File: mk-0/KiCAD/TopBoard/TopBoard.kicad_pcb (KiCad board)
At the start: 2 copper layers, 88 x 88 mm, 177 parts, among them J1 Conn_01x04, J2 Conn_01x04, J3 USB_C_Receptacle_USB2.0_16P, J4 Conn_01x15, J5 Raspberry_Pi_2_3, Q1 AO3400A, SW1 SW_Push, SW2 SW_Push, SW3 SW_Push, SW4 SW_Push, U1 SN74LVC1G126DBV, U10 SRV05-4, U11 AMS1117-1.2, U2 74LVC1G17, U3 SN74LVC2G74, U4 74AHCT1G125, U5 W25Q16JVSS, U6 CAT24C256, U7 SN74LVC1G126DBV, U8 ZL38063, U9 AMS1117-3.3, Y1 12MHz

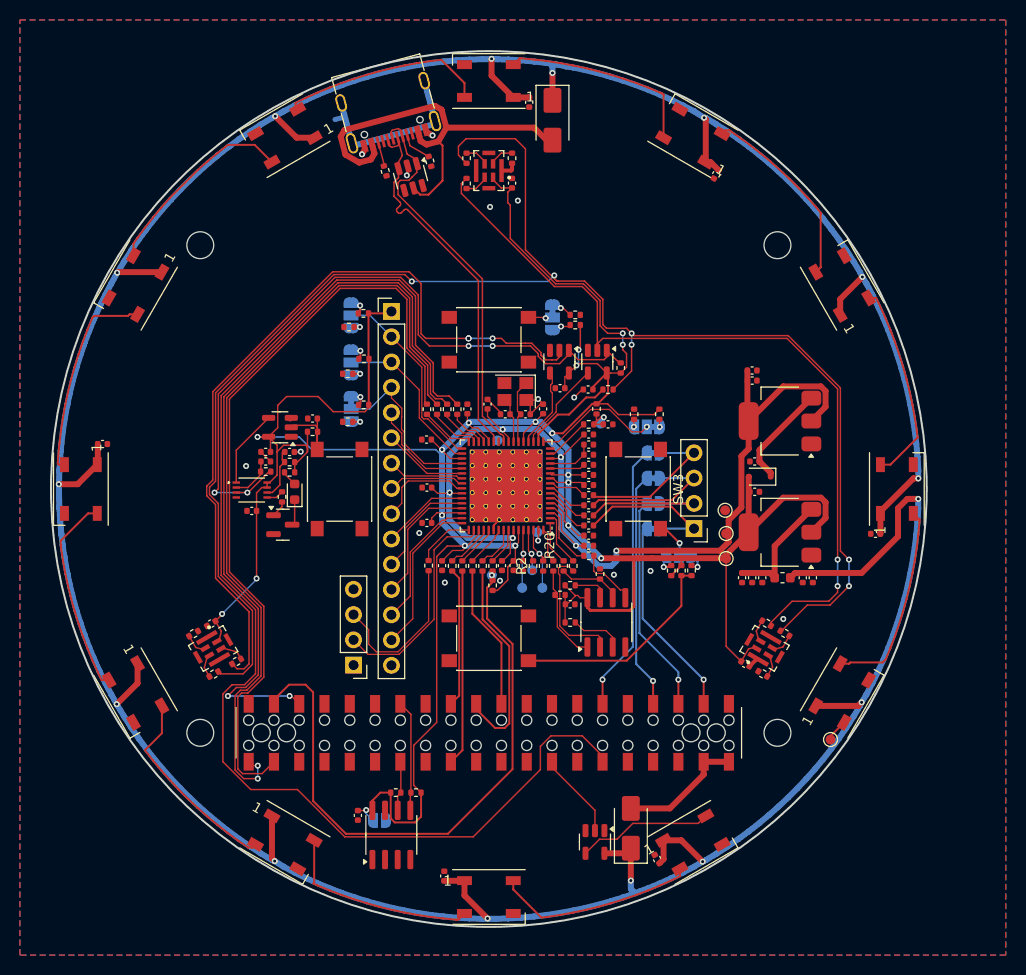
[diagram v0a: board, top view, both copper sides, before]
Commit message: Full routed and DRC completed
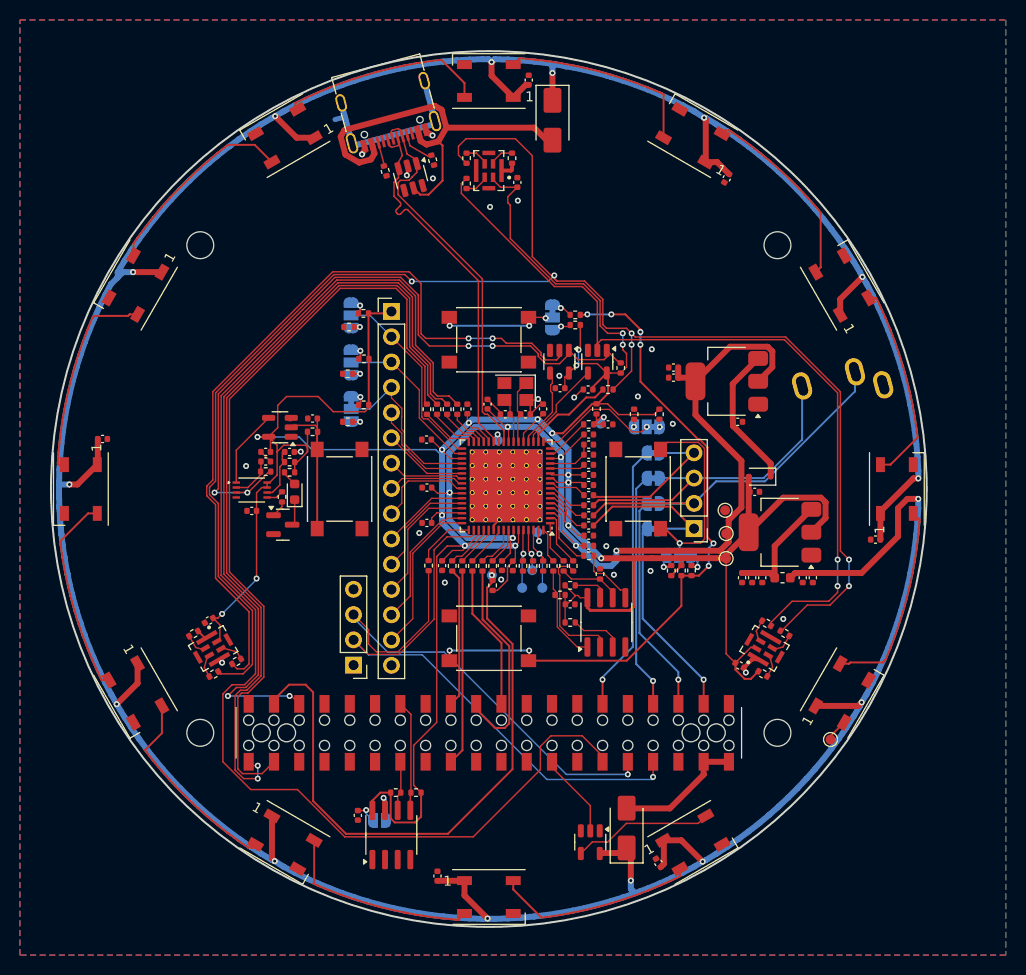
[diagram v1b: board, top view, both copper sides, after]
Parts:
- added J6: AudioJack3, Connector_Audio:Jack_3.5mm_CUI_SJ1-3533NG_Horizontal, B.Cu at (124.8, 59.5)
- moved C47 8.02 mm to (103.8, 57.8), turned to 180 degrees
- moved C49 7.94 mm to (103.8, 58.8), turned to 180 degrees
- moved U11 6.67 mm to (109.1, 59.2)
- moved C45 4.34 mm to (110.2, 63.2), turned to 0 degrees
- moved C28 2.24 mm to (89.2, 28.9), turned to 90 degrees
- moved C22 1.13 mm to (109.1, 38.8)
- moved C39 0.69 mm to (80.1, 108.9)
- moved C41 0.61 mm to (110.4, 87.7)
- moved C38 0.58 mm to (124.1, 75.1)
- moved C40 0.54 mm to (88.1, 39.2)
- moved C32 0.51 mm to (46.4, 65.0)
- moved U4 0.47 mm to (95.4, 105.5)
- moved D16 0.43 mm to (99.1, 104.1)
- moved C37 0.40 mm to (102.3, 107.6)
- moved C42 0.38 mm to (57.1, 83.2)
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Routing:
- net BTN3: track 21.7 -> 67.7 mm, vias 0 -> 8
- net ZL38063_UART_RX: track 22.2 -> 59.9 mm, vias 0 -> 1
- net ZL38063_UART_TX: track 16.3 -> 51.6 mm, vias 0 -> 1
- net ZL38063_DAC1_P: track 14.0 -> 36.8 mm
- net ZL38063_DAC2_P: track 14.7 -> 32.5 mm
- net Net-(JP11-C): track 2.86 -> 19.6 mm
- net Net-(JP10-C): track 1.76 -> 11.3 mm, vias 1 -> 3
- net Net-(C2-Pad1): track 7.19 -> 15.1 mm
- net +3V3: track 331.5 -> 336.9 mm
- net Net-(D15-K): track 10.5 -> 14.5 mm
- net +5V: track 366.7 -> 370.6 mm
- net Net-(JP1-A): track 0.00 -> 3.47 mm, vias 0 -> 1
- net +1V2: track 106.9 -> 110.1 mm
- net GND: track 15.4 -> 18.4 mm, vias 15 -> 23
- net Net-(U8-RTN): track 0.00 -> 1.35 mm, vias 0 -> 1
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
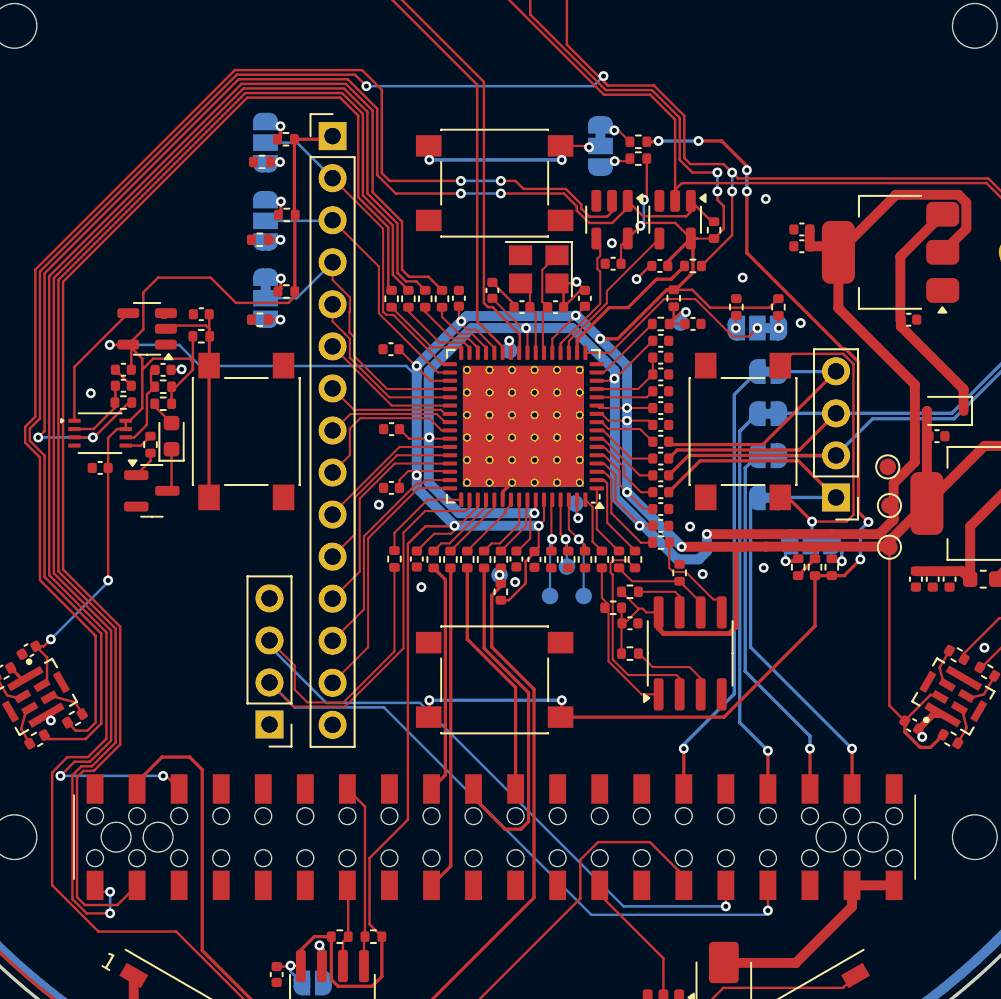
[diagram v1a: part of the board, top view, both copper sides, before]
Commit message: Added 3.5mm Jack to top board
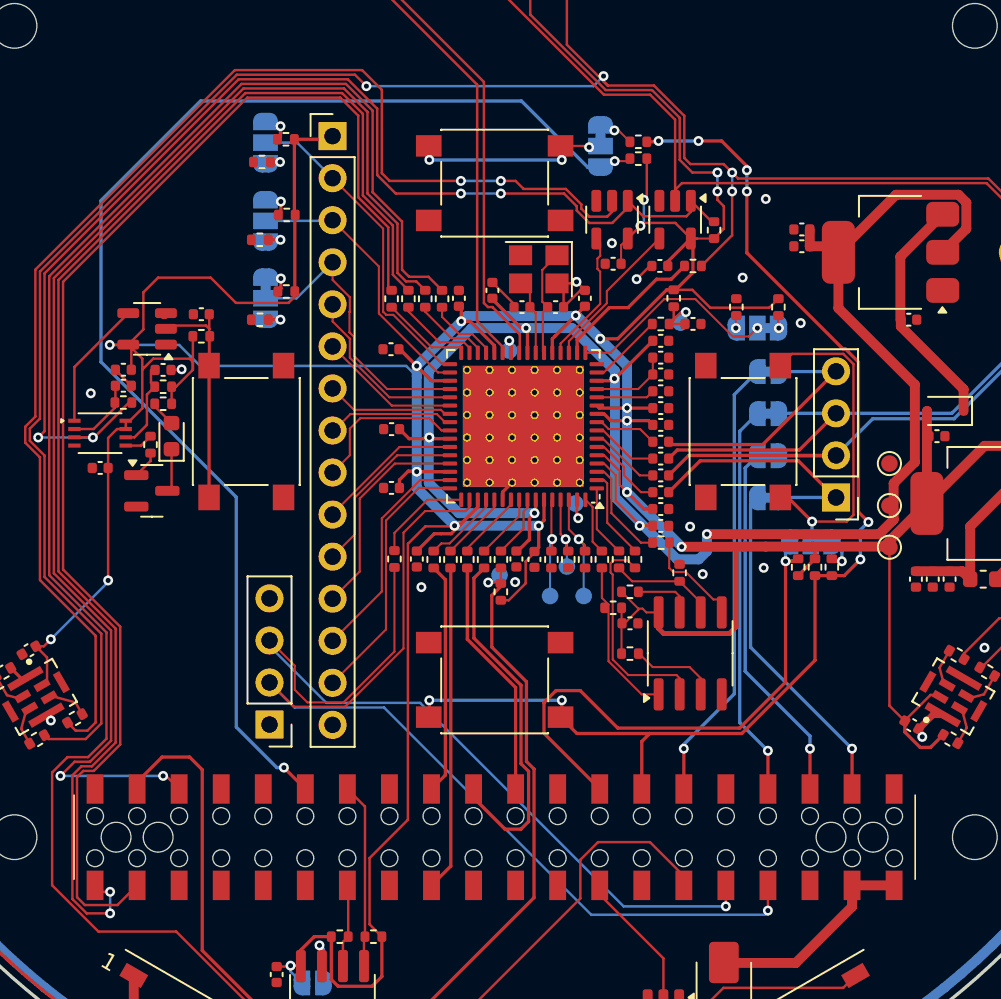
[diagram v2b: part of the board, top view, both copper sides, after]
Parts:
- moved TP11 0.23 mm to (109.1, 71.9)
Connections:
- J5 pad 13: unconnected-(J5-GPIO27-Pad13) -> BTN3
- J5 pad 15: unconnected-(J5-GPIO22-Pad15) -> BTN2
- J5 pad 29: unconnected-(J5-GCLK1/GPIO5-Pad29) -> BTN1
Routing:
- net BTN1: track 0.77 -> 76.0 mm, vias 1 -> 2
- net BTN2: track 2.00 -> 32.9 mm
- net +3V3: track 336.9 -> 351.4 mm
- net BTN3: track 67.7 -> 73.3 mm
- net +1V2: track 110.1 -> 115.4 mm
- net ZL38063_HINT: track 62.1 -> 62.9 mm
- net ZL38063_SPI_HDOUT: track 20.7 -> 21.2 mm
- net GND: vias 23 -> 22

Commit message: Cleanup and naming of Touchpoints
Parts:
- added TP13: GPIO7, TestPoint:TestPoint_Pad_D1.0mm, B.Cu at (78.9, 100.6)
- added TP14: GPIO12, TestPoint:TestPoint_Pad_D1.0mm, B.Cu at (71.2, 100.7)
- added TP15: GPIO16, TestPoint:TestPoint_Pad_D1.0mm, B.Cu at (66.2, 100.7)
- added TP16: GPIO24, TestPoint:TestPoint_Pad_D1.0mm, B.Cu at (89.0, 100.7)
- added TP17: GPIO25, TestPoint:TestPoint_Pad_D1.0mm, B.Cu at (84.0, 100.6)
- added TP9: GPIO6, TestPoint:TestPoint_Pad_D1.0mm, B.Cu at (68.8, 100.7)
- SW1: value SW_Push -> MUTE
- SW2: value SW_Push -> BUTTON 1
- SW3: value SW_Push -> BUTTON 2
- SW4: value SW_Push -> BUTTON 3
- TP10: value TestPoint -> 1V2
- TP11: value TestPoint -> GND
- TP7: value TestPoint -> 3V3
- moved C28 21.4 mm to (68.2, 32.6), turned to 120 degrees
- moved C39 19.5 mm to (61.4, 103.4), turned to -120 degrees
- moved TP10 8.64 mm to (109.1, 65.8)
- moved J1 7.61 mm to (71.6, 80.1), turned to 0 degrees
- moved TP4 6.73 mm to (93.7, 80.0)
- moved NT2 4.78 mm to (74.7, 30.9), turned to 105 degrees
- moved C32 2.36 mm to (44.3, 66.0), turned to 180 degrees
- moved C22 2.25 mm to (109.1, 36.5), turned to 60 degrees
- moved C38 2.07 mm to (125.8, 73.9), turned to 0 degrees
- moved TP11 1.93 mm to (109.1, 70.0)
- moved TP2 1.86 mm to (89.7, 80.0)
- moved TP5 1.35 mm to (85.5, 80.0)
- moved TP3 1.09 mm to (91.7, 80.0)
- moved TP1 0.94 mm to (87.6, 80.0)
- moved C37 0.23 mm to (102.2, 107.3), turned to -60 degrees
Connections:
- net /Power/PIN11 renamed Net-(J5-GPIO17)
- net /Power/PIN3 renamed Net-(J5-SDA/GPIO2)
- net /Power/PIN5 renamed Net-(J5-SCL/GPIO3)
- net /Power/PIN7 renamed Net-(J5-GCLK0/GPIO4)
- J1 pad 1: unconnected-(J1-Pin_1-Pad1) -> GND
- J1 pad 2: ZL38063_UART_RX -> ZL38063_UART_TX
- J1 pad 3: ZL38063_UART_TX -> ZL38063_UART_RX
- J1 pad 4: GND -> +3V3
- J5 pad 18: unconnected-(J5-GPIO24-Pad18) -> Net-(J5-GPIO24)
- J5 pad 22: unconnected-(J5-GPIO25-Pad22) -> Net-(J5-GPIO25)
- J5 pad 26: unconnected-(J5-~{CE1}/GPIO7-Pad26) -> Net-(J5-~{CE1}/GPIO7)
- J5 pad 31: unconnected-(J5-GCLK2/GPIO6-Pad31) -> Net-(J5-GCLK2/GPIO6)
- J5 pad 32: unconnected-(J5-PWM0/GPIO12-Pad32) -> Net-(J5-PWM0/GPIO12)
- J5 pad 33: unconnected-(J5-PWM1/GPIO13-Pad33) -> MUTE_PWR
- J5 pad 36: unconnected-(J5-GPIO16-Pad36) -> Net-(J5-GPIO16)
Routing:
- net MUTE_PWR: track 1.73 -> 24.8 mm
- net BTN1: track 76.0 -> 54.2 mm
- net Net-(J5-GCLK2/GPIO6): track 0.00 -> 10.1 mm, vias 0 -> 1
- net ZL38063_DMIC_CLK: track 167.1 -> 173.1 mm
- net Net-(U8-DXB/I2S_SDOB): track 2.00 -> 7.35 mm
- net ZL38063_DAC2_M: track 15.2 -> 18.6 mm
- net Net-(J5-PWM0/GPIO12): track 0.00 -> 3.28 mm, vias 0 -> 1
- net Net-(J5-GPIO16): track 0.00 -> 3.27 mm, vias 0 -> 1
- net Net-(J5-GPIO25): track 0.00 -> 3.23 mm, vias 0 -> 1
- net Net-(J5-~{CE1}/GPIO7): track 0.00 -> 3.23 mm, vias 0 -> 1
- net Net-(J5-GPIO24): track 0.00 -> 3.22 mm, vias 0 -> 1
- net /Interface/MUTE_DATA: track 70.8 -> 72.6 mm
- net ZL38063_DAC1_P: track 36.8 -> 38.5 mm
- net Net-(U8-FSB/I2S_WSB): track 4.78 -> 6.45 mm
- net +5V: track 370.6 -> 369.1 mm
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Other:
- board text added: "3V3 0 1 2 3 4 5 6 7 8 10 11 12 13 GND"
- board text added: "DAC Passthrough. Break for RPi"
- board text added: "ESP32|RPi"
- board text added: "GPIO12"
- board text added: "GPIO16"
- board text added: "GPIO24"
- board text added: "GPIO25"
- board text added: "GPIO6"
- board text added: "GPIO7"
- board text added: "HINT"
- board text added: "I2S_SCKB"
- board text added: "I2S_SDIB"
- board text added: "I2S_SDOB"
- board text added: "I2S_WSB"
- board text added: "ID_WP"
- board text added: "LibreTalk Wave HAT V1.0 04/2024"
- board text added: "UART"

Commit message: Silkscreen text alignment
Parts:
- moved J4 35.6 mm to (75.4, 87.7), turned to 180 degrees
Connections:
- J4 pad 1: +3V3 -> GND
- J4 pad 12: Net-(J4-Pin_12) -> /DSP/GPIO2
- J4 pad 13: Net-(J4-Pin_13) -> /DSP/GPIO1
- J4 pad 14: Net-(J4-Pin_14) -> /DSP/GPIO0
- J4 pad 15: GND -> +3V3
- J4 pad 2: /DSP/GPIO0 -> Net-(J4-Pin_2)
- J4 pad 3: /DSP/GPIO1 -> Net-(J4-Pin_3)
- J4 pad 4: /DSP/GPIO2 -> Net-(J4-Pin_4)
- U8 pad 37: Net-(J4-Pin_5) -> Net-(J4-Pin_11)
- U8 pad 38: Net-(J4-Pin_6) -> Net-(J4-Pin_10)
- U8 pad 39: Net-(J4-Pin_7) -> Net-(J4-Pin_9)
- U8 pad 41: Net-(J4-Pin_9) -> Net-(J4-Pin_7)
- U8 pad 43: Net-(J4-Pin_10) -> Net-(J4-Pin_6)
- U8 pad 44: Net-(J4-Pin_11) -> Net-(J4-Pin_5)
- U8 pad 45: Net-(J4-Pin_12) -> Net-(J4-Pin_4)
- U8 pad 47: Net-(J4-Pin_13) -> Net-(J4-Pin_3)
- U8 pad 48: Net-(J4-Pin_14) -> Net-(J4-Pin_2)
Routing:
- net Net-(J4-Pin_2): track 0.00 -> 15.8 mm
- net Net-(J4-Pin_14): track 15.8 -> 0.00 mm
- net Net-(J4-Pin_3): track 0.00 -> 13.7 mm
- net Net-(J4-Pin_13): track 13.7 -> 0.00 mm
- net Net-(J4-Pin_4): track 0.00 -> 13.0 mm
- net Net-(J4-Pin_12): track 13.0 -> 0.00 mm
- net Net-(J4-Pin_9): track 9.69 -> 7.42 mm
- net Net-(J4-Pin_7): track 7.42 -> 9.69 mm
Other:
- board text added: "+ GPIO0 -"
- board text added: "+ GPIO1 -"
- board text added: "+ GPIO2 -"
- board text added: "DAC1+"
- board text added: "DAC1-"
- board text added: "DAC2+"
- board text added: "DAC2-"
- board text added: "EXT_SEL"
- board text added: "RESET"
- board text added: "RTN"
